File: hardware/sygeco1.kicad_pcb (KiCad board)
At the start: 2 copper layers, 30.5 x 73 mm, 25 parts, among them J1 SSD1306_module, J2 AVR-ISP-6, SW1 SW_Push_DPDT, SW2 SW_Push_DPDT, U1 ATtiny85-20PU

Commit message: update revision (1.0)
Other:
- board text added: "Version 1.0"
- board text removed: "Version 0.2"

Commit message: migrated files to kicad 6.0 (-rc1)
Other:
- net class Default removed

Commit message: add 3d model for DPDT switches
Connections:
- SW1 pad 1: Net-(SW1-Pad1) -> unconnected-(SW1-Pad1)
- SW1 pad 4: Net-(SW1-Pad4) -> unconnected-(SW1-Pad4)
- SW2 pad 1: Net-(SW2-Pad1) -> unconnected-(SW2-Pad1)
- SW2 pad 4: Net-(SW2-Pad4) -> unconnected-(SW2-Pad4)

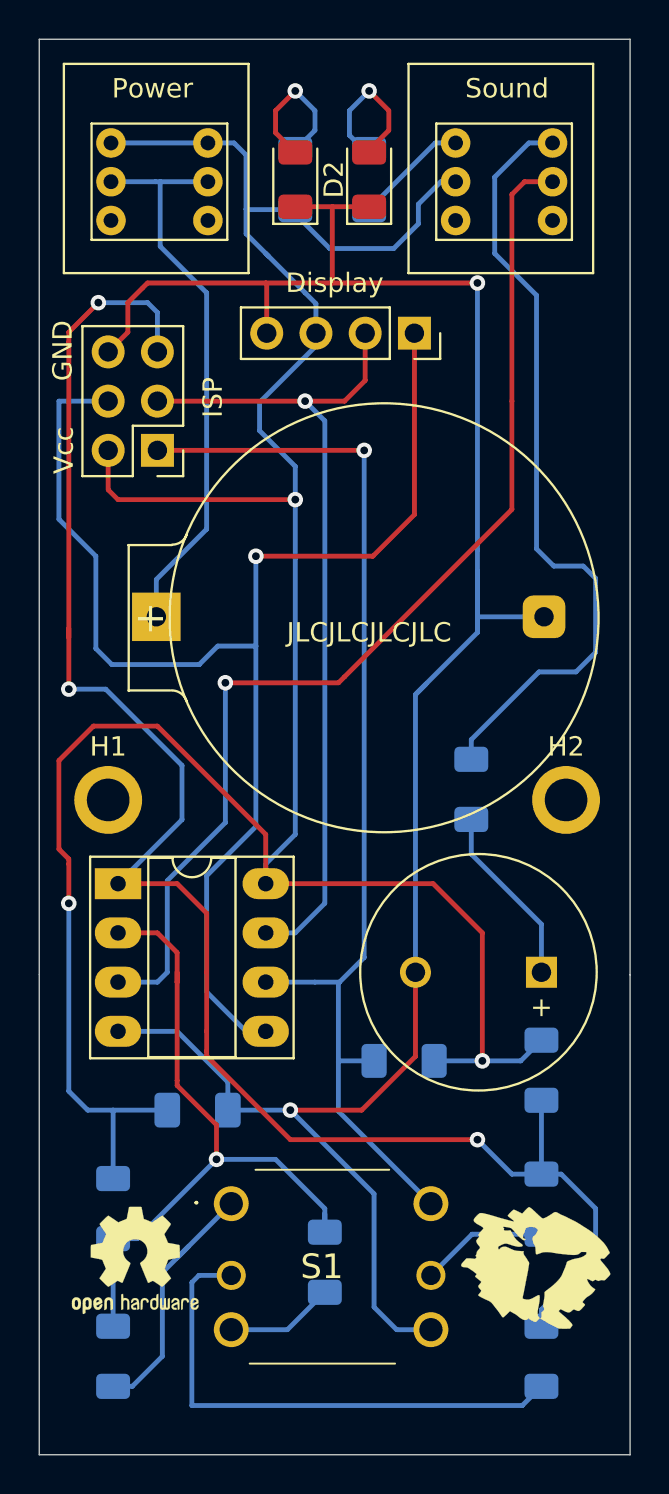
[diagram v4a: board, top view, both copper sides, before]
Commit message: Add some (silicone) pads. pcb: cleaning all errors/warnings
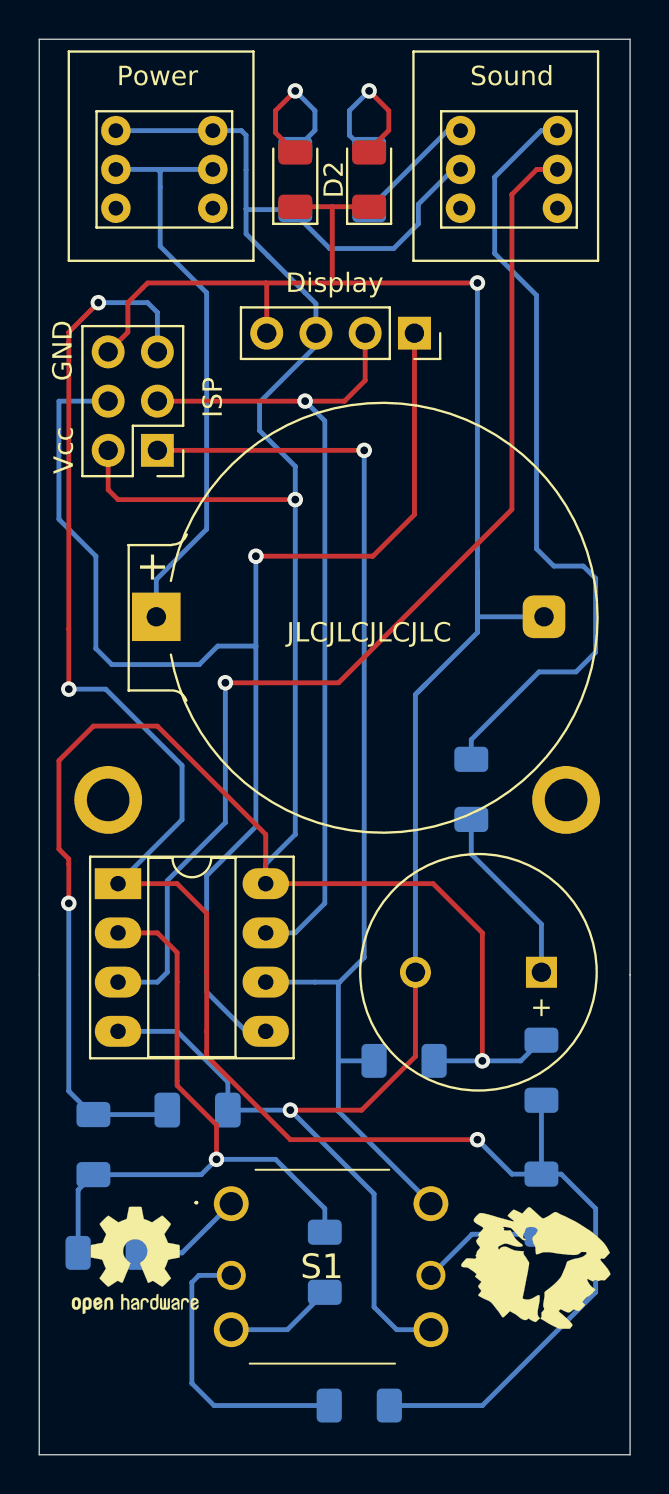
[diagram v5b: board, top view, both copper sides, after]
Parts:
- added RP1: silicone_rubber_pad, sygeco:silicone_rubber_pad, B.Cu at (152.0, 61.3)
- added RP2: silicone_rubber_pad, sygeco:silicone_rubber_pad, B.Cu at (131.1, 116.7)
- added RP3: silicone_rubber_pad, sygeco:silicone_rubber_pad, B.Cu at (133.3, 60.0)
- added RP4: silicone_rubber_pad, sygeco:silicone_rubber_pad, B.Cu at (153.5, 116.7)
- moved R8 9.74 mm to (143.5, 124.5), turned to 180 degrees
- moved R1 5.34 mm to (130.6, 116.6), turned to 0 degrees
- moved R4 3.45 mm to (129.8, 111.0)
- moved SW1 0.68 mm to (140.0, 59.7)
- moved SW2 0.68 mm to (157.7, 59.7)
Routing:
- net Net-(R8-Pad2): track 27.5 -> 14.9 mm
- net PAD_AXIS_1: track 88.4 -> 97.9 mm
- net Net-(R1-Pad2): track 13.3 -> 5.85 mm
- net PAD_AXIS_2: track 37.4 -> 33.9 mm
- net VCC: track 142.1 -> 139.7 mm
- net Net-(BT1-Pad1): track 30.8 -> 30.2 mm
- net Net-(SW2-Pad5): track 56.0 -> 56.6 mm
- net Net-(R9-Pad1): track 5.90 -> 6.42 mm
- net Net-(R10-Pad2): track 40.6 -> 41.1 mm
- net GND: track 114.9 -> 114.4 mm
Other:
- board text added: "Version 1.1"
- board text removed: "Version 1.0"

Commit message: Better align pads
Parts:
- moved RP1 1.66 mm to (151.1, 59.9)
- moved RP3 0.13 mm to (133.3, 59.9)
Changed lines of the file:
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@@
   )
   (footprint "sygeco:silicone_rubber_pad" (layer "B.Cu")
-    (at 152.019 61.254 180)
+    (at 151.13 59.857 180)
     (property "Sheetfile" "sygeco1.kicad_sch")
     (property "Sheetname" "")
@@
   )
   (footprint "sygeco:silicone_rubber_pad" (layer "B.Cu")
-    (at 133.35 59.984 180)
+    (at 133.35 59.857 180)
     (property "Sheetfile" "sygeco1.kicad_sch")
     (property "Sheetname" "")

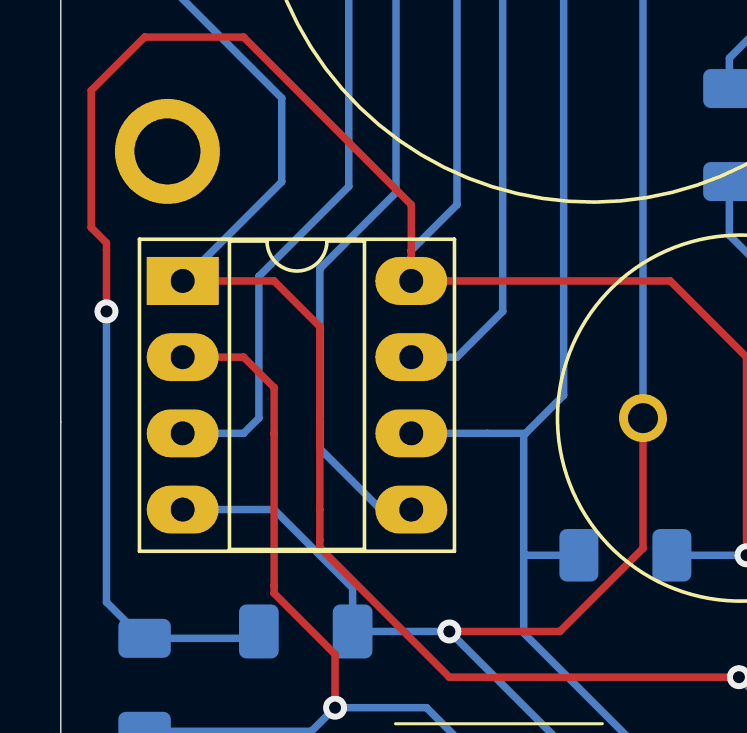
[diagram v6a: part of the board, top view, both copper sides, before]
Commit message: Fix attiny85 symbol + all errors/warnings. Seems like my symbol was obsolate..(?)
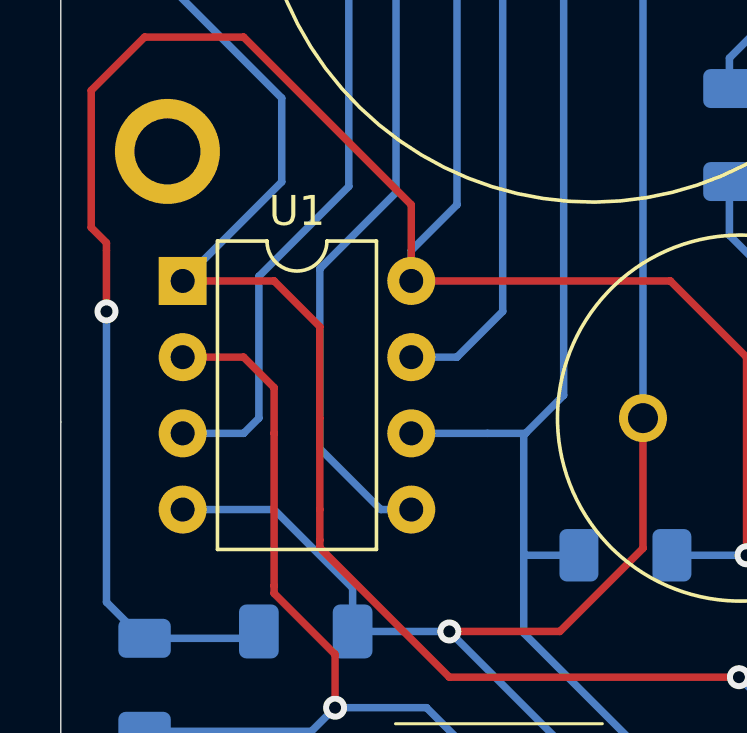
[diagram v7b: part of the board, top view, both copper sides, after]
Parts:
- U1: value ATtiny85-20PU -> ATtiny85-20P; footprint Package_DIP:DIP-8_W7.62mm_Socket_LongPads -> Package_DIP:DIP-8_W7.62mm
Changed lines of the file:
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@@
-    )
-  )
-  (footprint "Package_DIP:DIP-8_W7.62mm_Socket_LongPads" (layer "F.Cu")
-    (at 131.064 97.536)
-    (descr "8-lead though-hole mounted DIP package, row spacing 7.62 mm (300 mils), Socket, LongPads")
-    (tags "THT DIP DIL PDIP 2.54mm 7.62mm 300mil Socket LongPads")
-    (property "Sheetfile" "sygeco1.kicad_sch")
-    (property "Sheetname" "")
-    (attr through_hole)
-    (fp_text reference "U1" (at 3.81 -2.33) (layer "F.SilkS") hide
-      (effects (font (size 1 1) (thickness 0.15)))
-    )
-    (fp_text value "ATtiny85-20PU" (at 3.81 9.95) (layer "F.Fab")
-      (effects (font (size 1 1) (thickness 0.15)))
-    )
-    (fp_text user "${REFERENCE}" (at 3.81 3.81) (layer "F.Fab")
-      (effects (font (size 1 1) (thickness 0.15)))
-    )
-    (fp_line (start 9.06 9.01) (end 9.06 -1.39) (layer "F.SilkS") (width 0.12))
-    (fp_line (start -1.44 9.01) (end 9.06 9.01) (layer "F.SilkS") (width 0.12))
-    (fp_line (start 1.56 8.95) (end 6.06 8.95) (layer "F.SilkS") (width 0.12))
-    (fp_line (start 1.56 -1.33) (end 1.56 8.95) (layer "F.SilkS") (width 0.12))
-    (fp_line (start 2.81 -1.33) (end 1.56 -1.33) (layer "F.SilkS") (width 0.12))
-    (fp_line (start -1.44 -1.39) (end -1.44 9.01) (layer "F.SilkS") (width 0.12))
-    (fp_line (start 6.06 -1.33) (end 4.81 -1.33) (layer "F.SilkS") (width 0.12))
-    (fp_line (start 6.06 8.95) (end 6.06 -1.33) (layer "F.SilkS") (width 0.12))
-    (fp_line (start 9.06 -1.39) (end -1.44 -1.39) (layer "F.SilkS") (width 0.12))
-    (fp_arc (start 4.81 -1.33) (mid 3.81 -0.33) (end 2.81 -1.33) (layer "F.SilkS") (width 0.12))
-    (fp_line (start 9.15 9.2) (end 9.15 -1.6) (layer "F.CrtYd") (width 0.05))
-    (fp_line (start 9.15 -1.6) (end -1.55 -1.6) (layer "F.CrtYd") (width 0.05))
-    (fp_line (start -1.55 9.2) (end 9.15 9.2) (layer "F.CrtYd") (width 0.05))
-    (fp_line (start -1.55 -1.6) (end -1.55 9.2) (layer "F.CrtYd") (width 0.05))
-    (fp_line (start 0.635 -0.27) (end 1.635 -1.27) (layer "F.Fab") (width 0.1))
-    (fp_line (start 1.635 -1.27) (end 6.985 -1.27) (layer "F.Fab") (width 0.1))
-    (fp_line (start 6.985 -1.27) (end 6.985 8.89) (layer "F.Fab") (width 0.1))
-    (fp_line (start 6.985 8.89) (end 0.635 8.89) (layer "F.Fab") (width 0.1))
-    (fp_line (start -1.27 8.95) (end 8.89 8.95) (layer "F.Fab") (width 0.1))
-    (fp_line (start 8.89 8.95) (end 8.89 -1.33) (layer "F.Fab") (width 0.1))
-    (fp_line (start 0.635 8.89) (end 0.635 -0.27) (layer "F.Fab") (width 0.1))
-    (fp_line (start 8.89 -1.33) (end -1.27 -1.33) (layer "F.Fab") (width 0.1))
-    (fp_line (start -1.27 -1.33) (end -1.27 8.95) (layer "F.Fab") (width 0.1))
-    (pad "1" thru_hole rect locked (at 0 0) (size 2.4 1.6) (drill 0.8) (layers *.Cu *.Mask)
-      (net 15 "PAD_AXIS_1") (pinfunction "~{RESET}/PB5") (pintype "bidirectional"))
-    (pad "2" thru_hole oval locked (at 0 2.54) (size 2.4 1.6) (drill 0.8) (layers *.Cu *.Mask)
-      (net 16 "PAD_AXIS_2") (pinfunction "XTAL1/PB3") (pintype "bidirectional"))
-    (pad "3" thru_hole oval locked (at 0 5.08) (size 2.4 1.6) (drill 0.8) (layers *.Cu *.Mask)
-      (net 19 "Net-(SW2-Pad5)") (pinfunction "XTAL2/PB4") (pintype "bidirectional"))
-    (pad "4" thru_hole oval locked (at 0 7.62) (size 2.4 1.6) (drill 0.8) (layers *.Cu *.Mask)
-      (net 2 "GND") (pinfunction "GND") (pintype "power_in"))
-    (pad "5" thru_hole oval locked (at 7.62 7.62) (size 2.4 1.6) (drill 0.8) (layers *.Cu *.Mask)
-      (net 3 "SDA") (pinfunction "AREF/PB0") (pintype "bidirectional"))
-    (pad "6" thru_hole oval locked (at 7.62 5.08) (size 2.4 1.6) (drill 0.8) (layers *.Cu *.Mask)
-      (net 8 "Button") (pinfunction "PB1") (pintype "bidirectional"))
-    (pad "7" thru_hole oval locked (at 7.62 2.54) (size 2.4 1.6) (drill 0.8) (layers *.Cu *.Mask)
-      (net 4 "SCL") (pinfunction "PB2") (pintype "bidirectional"))
-    (pad "8" thru_hole oval locked (at 7.62 0) (size 2.4 1.6) (drill 0.8) (layers *.Cu *.Mask)
-      (net 5 "VCC") (pinfunction "VCC") (pintype "power_in"))
-    (model "${KISYS3DMOD}/Package_DIP.3dshapes/DIP-8_W7.62mm_Socket.wrl"
-      (offset (xyz 0 0 0))
-      (scale (xyz 1 1 1))
-      (rotate (xyz 0 0 0))
     )
   )
@@
     )
   )
+  (footprint "Package_DIP:DIP-8_W7.62mm" (layer "F.Cu")
+    (at 131.064 97.536)
+    (descr "8-lead though-hole mounted DIP package, row spacing 7.62 mm (300 mils)")
+    (tags "THT DIP DIL PDIP 2.54mm 7.62mm 300mil")
+    (property "Sheetfile" "sygeco1.kicad_sch")
+    (property "Sheetname" "")
+    (attr through_hole)
+    (fp_text reference "U1" (at 3.81 -2.33) (layer "F.SilkS")
+      (effects (font (size 1 1) (thickness 0.15)))
+    )
+    (fp_text value "ATtiny85-20P" (at 3.81 9.95) (layer "F.Fab")
+      (effects (font (size 1 1) (thickness 0.15)))
+    )
+    (fp_text user "${REFERENCE}" (at 3.81 3.81) (layer "F.Fab")
+      (effects (font (size 1 1) (thickness 0.15)))
+    )
+    (fp_line (start 1.16 -1.33) (end 1.16 8.95) (layer "F.SilkS") (width 0.12))
+    (fp_line (start 6.46 -1.33) (end 4.81 -1.33) (layer "F.SilkS") (width 0.12))
+    (fp_line (start 6.46 8.95) (end 6.46 -1.33) (layer "F.SilkS") (width 0.12))
+    (fp_line (start 2.81 -1.33) (end 1.16 -1.33) (layer "F.SilkS") (width 0.12))
+    (fp_line (start 1.16 8.95) (end 6.46 8.95) (layer "F.SilkS") (width 0.12))
+    (fp_arc (start 4.81 -1.33) (mid 3.81 -0.33) (end 2.81 -1.33) (layer "F.SilkS") (width 0.12))
+    (fp_line (start 8.7 9.15) (end 8.7 -1.55) (layer "F.CrtYd") (width 0.05))
+    (fp_line (start -1.1 -1.55) (end -1.1 9.15) (layer "F.CrtYd") (width 0.05))
+    (fp_line (start -1.1 9.15) (end 8.7 9.15) (layer "F.CrtYd") (width 0.05))
+    (fp_line (start 8.7 -1.55) (end -1.1 -1.55) (layer "F.CrtYd") (width 0.05))
+    (fp_line (start 1.635 -1.27) (end 6.985 -1.27) (layer "F.Fab") (width 0.1))
+    (fp_line (start 6.985 8.89) (end 0.635 8.89) (layer "F.Fab") (width 0.1))
+    (fp_line (start 0.635 -0.27) (end 1.635 -1.27) (layer "F.Fab") (width 0.1))
+    (fp_line (start 6.985 -1.27) (end 6.985 8.89) (layer "F.Fab") (width 0.1))
+    (fp_line (start 0.635 8.89) (end 0.635 -0.27) (layer "F.Fab") (width 0.1))
+    (pad "1" thru_hole rect (at 0 0) (size 1.6 1.6) (drill 0.8) (layers *.Cu *.Mask)
+      (net 15 "PAD_AXIS_1") (pinfunction "~{RESET}/PB5") (pintype "bidirectional"))
+    (pad "2" thru_hole oval (at 0 2.54) (size 1.6 1.6) (drill 0.8) (layers *.Cu *.Mask)
+      (net 16 "PAD_AXIS_2") (pinfunction "XTAL1/PB3") (pintype "bidirectional"))
+    (pad "3" thru_hole oval (at 0 5.08) (size 1.6 1.6) (drill 0.8) (layers *.Cu *.Mask)
+      (net 19 "Net-(SW2-Pad5)") (pinfunction "XTAL2/PB4") (pintype "bidirectional"))
+    (pad "4" thru_hole oval (at 0 7.62) (size 1.6 1.6) (drill 0.8) (layers *.Cu *.Mask)
+      (net 2 "GND") (pinfunction "GND") (pintype "power_in"))
+    (pad "5" thru_hole oval (at 7.62 7.62) (size 1.6 1.6) (drill 0.8) (layers *.Cu *.Mask)
+      (net 3 "SDA") (pinfunction "AREF/PB0") (pintype "bidirectional"))
+    (pad "6" thru_hole oval (at 7.62 5.08) (size 1.6 1.6) (drill 0.8) (layers *.Cu *.Mask)
+      (net 8 "Button") (pinfunction "PB1") (pintype "bidirectional"))
+    (pad "7" thru_hole oval (at 7.62 2.54) (size 1.6 1.6) (drill 0.8) (layers *.Cu *.Mask)
+      (net 4 "SCL") (pinfunction "PB2") (pintype "bidirectional"))
+    (pad "8" thru_hole oval (at 7.62 0) (size 1.6 1.6) (drill 0.8) (layers *.Cu *.Mask)
+      (net 5 "VCC") (pinfunction "VCC") (pintype "power_in"))
+    (model "${KICAD6_3DMODEL_DIR}/Package_DIP.3dshapes/DIP-8_W7.62mm.wrl"
+      (offset (xyz 0 0 0))
+      (scale (xyz 1 1 1))
+      (rotate (xyz 0 0 0))
+    )
+  )
